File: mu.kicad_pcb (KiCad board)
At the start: 4 copper layers, 60 x 60 mm, 75 parts, among them J1 USB_C_Receptacle_USB2.0_16P, J2 Conn_02x03_Odd_Even, J4 2060-1452/998-404, J5 ESQ-110-X-X-D, U1 STM32F042F6P6, U10 TLV3603QDCKRQ1, U11 SN74LVC1G74DCUT, U12 LM4040AIM3-2.5/NOPB, U13 MCP4921-E/SN, U14 BMP390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

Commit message: routed fully, pending final checks
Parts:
- moved C21 0.50 mm to (146.5, 67.0), turned to 180 degrees
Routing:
- net SPI_CS_FLASH: track 10.7 -> 9.67 mm

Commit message: ready for review
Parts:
- added G***: LOGO, LOGO, F.Cu at (144.2, 79.0)
- added G***: LOGO, LOGO, F.Cu at (146.0, 80.0)
- added G***: LOGO, LOGO, B.Cu at (179.5, 89.5)
- added G***: LOGO, LOGO, B.Cu at (156.0, 79.0)
- added G***: LOGO, LOGO, B.Cu at (167.5, 72.5)
- added G***: LOGO, LOGO, B.Cu at (167.0, 101.0)
- added G***: LOGO, LOGO, B.Cu at (138.5, 75.0)
- added G***: LOGO, LOGO, B.Cu at (146.5, 79.0)
- added REF**: WEEE-Logo_5.6x8mm_SilkScreen, Symbol:WEEE-Logo_5.6x8mm_SilkScreen, B.Cu at (147.5, 55.5)
- added REF**: ESD-Logo_6.6x6mm_SilkScreen, Symbol:ESD-Logo_6.6x6mm_SilkScreen, B.Cu at (166.5, 55.5)

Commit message: programming stuff
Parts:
- added J3: Conn_02x03_Odd_Even, Connector_PinHeader_1.00mm:PinHeader_2x03_P1.00mm_Vertical, F.Cu at (154.4, 88.0)
- moved R10 0.88 mm to (152.0, 86.6)
- moved R12 0.88 mm to (154.5, 86.2)
- moved R13 0.88 mm to (155.5, 86.2)
- moved R6 0.33 mm to (156.1, 84.2)
- moved U1 0.33 mm to (160.0, 87.7)
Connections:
- net Net-(U1A-NRST) renamed NRST
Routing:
- net NRST: track 2.68 -> 8.94 mm, vias 0 -> 1
- net 3.3V_Dig: track 130.3 -> 136.2 mm
- net SWCLK: track 0.68 -> 4.65 mm
- net SWDIO: track 1.79 -> 4.56 mm
- net GND: track 49.6 -> 52.0 mm
- net VBUS_RAW: track 60.1 -> 60.9 mm

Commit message: indeed
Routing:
- net 3.3V_Dig: track 136.2 -> 130.9 mm, vias 10 -> 9
- net GND: vias 54 -> 63
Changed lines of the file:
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@@
+	)
+	(via
+		(at 145 96)
+		(size 0.6)
+		(drill 0.3)
+		(layers "F.Cu" "B.Cu")
+		(free yes)
+		(net 1)
 	)
 	(via
@@
 	)
 	(via
+		(at 154.5 93)
+		(size 0.6)
+		(drill 0.3)
+		(layers "F.Cu" "B.Cu")
+		(free yes)
+		(net 1)
+	)
+	(via
 		(at 150.5 60)
 		(size 0.6)
@@
 	)
 	(via
+		(at 141 82)
+		(size 0.6)
+		(drill 0.3)
+		(layers "F.Cu" "B.Cu")
+		(free yes)
+		(net 1)
+	)
+	(via
+		(at 170.5 67)
+		(size 0.6)
+		(drill 0.3)
+		(layers "F.Cu" "B.Cu")
+		(free yes)
+		(net 1)
+	)
+	(via
 		(at 155 72)
 		(size 0.6)
@@
 	)
 	(via
+		(at 159.5 63)
+		(size 0.6)
+		(drill 0.3)
+		(layers "F.Cu" "B.Cu")
+		(free yes)
+		(net 1)
+	)
+	(via
 		(at 146.575 59.356)
 		(size 0.6)
@@
 	)
 	(via
-		(at 163.545601 63.4861)
+		(at 152 83)
 		(size 0.6)
 		(drill 0.3)
@@
 	)
 	(via
+		(at 170.5 76.5)
+		(size 0.6)
+		(drill 0.3)
+		(layers "F.Cu" "B.Cu")
+		(free yes)
+		(net 1)
+	)
+	(via
 		(at 155.54 68.75)
 		(size 0.6)
@@
 	)
 	(via
+		(at 154.5 55.5)
+		(size 0.6)
+		(drill 0.3)
+		(layers "F.Cu" "B.Cu")
+		(free yes)
+		(net 1)
+	)
+	(via
 		(at 148.595 62.336)
 		(size 0.6)
@@
 	)
 	(via
+		(at 141 88.5)
+		(size 0.6)
+		(drill 0.3)
+		(layers "F.Cu" "B.Cu")
+		(free yes)
+		(net 1)
+	)
+	(via
 		(at 161 88.5)
 		(size 0.6)
@@
 		(layers "F.Cu" "B.Cu")
 		(free yes)
+		(net 1)
+	)
+	(via
+		(at 184 72.952)
+		(size 0.6)
+		(drill 0.3)
+		(layers "F.Cu" "B.Cu")
 		(net 1)
 	)
@@
 	)
 	(segment
+		(start 184 72.952)
+		(end 183.02 72.952)
+		(width 0.6)
+		(layer "B.Cu")
+		(net 1)
+	)
+	(segment
 		(start 159.711326 100.383399)
 		(end 159.711326 98.738399)
@@
 	(segment
 		(start 184.024 72.952)
-		(end 183.02 72.952)
+		(end 184 72.952)
 		(width 0.6)
 		(layer "B.Cu")
@@
 	)
 	(via
-		(at 148 74.5)
-		(size 0.6)
-		(drill 0.3)
-		(layers "F.Cu" "B.Cu")
-		(net 2)
-	)
-	(via
 		(at 159.474999 94.579)
 		(size 0.6)
@@
 	)
 	(segment
-		(start 148 74.5)
-		(end 147 75.5)
-		(width 0.25)
-		(layer "In1.Cu")
-		(net 2)
-	)
-	(segment
-		(start 157.5 73.5)
-		(end 157.5 71.75)
-		(width 0.25)
-		(layer "In1.Cu")
-		(net 2)
-	)
-	(segment
 		(start 166.293225 91.600756)
 		(end 164.915981 92.978)
@@
 	(segment
 		(start 157.5 71.75)
-		(end 156 70.25)
+		(end 157.5 75)
 		(width 0.25)
 		(layer "In1.Cu")
@@
 	)
 	(segment
+		(start 156 70.25)
+		(end 157.5 71.75)
+		(width 0.25)
+		(layer "In1.Cu")
+		(net 2)
+	)
+	(segment
 		(start 170 82.5)
 		(end 171 82.5)
@@
 	)
 	(segment
-		(start 157.101 73.899)
-		(end 152.101 73.899)
-		(width 0.25)
-		(layer "In1.Cu")
-		(net 2)
-	)
-	(segment
 		(start 166.293225 91.600756)
 		(end 166.5 91.393981)
@@
 	)
 	(segment
-		(start 152.101 73.899)
-		(end 151.5 74.5)
-		(width 0.25)
-		(layer "In1.Cu")
-		(net 2)
-	)
-	(segment
 		(start 159.299999 70.25)
 		(end 156 70.25)
@@
 	)
 	(segment
-		(start 157.5 73.5)
-		(end 157.101 73.899)
+		(start 157.5 75)
+		(end 147.5 85)
 		(width 0.25)
 		(layer "In1.Cu")
@@
 	)
 	(segment
+		(start 147.5 90.840598)
+		(end 147.365 90.975598)
+		(width 0.25)
+		(layer "In1.Cu")
+		(net 2)
+	)
+	(segment
 		(start 162 67.549999)
 		(end 159.299999 70.25)
@@
 	)
 	(segment
-		(start 147 75.5)
-		(end 147 90.610598)
-		(width 0.25)
-		(layer "In1.Cu")
-		(net 2)
-	)
-	(segment
 		(start 159.474999 94.579)
 		(end 160.075999 95.18)
@@
 	)
 	(segment
-		(start 151.5 74.5)
-		(end 148 74.5)
-		(width 0.25)
-		(layer "In1.Cu")
-		(net 2)
-	)
-	(segment
 		(start 163.05454 93.488)
 		(end 162.556654 93.488)
@@
 	)
 	(segment
+		(start 147.5 85)
+		(end 147.5 90.840598)
+		(width 0.25)
+		(layer "In1.Cu")
+		(net 2)
+	)
+	(segment
 		(start 162.556654 93.488)
 		(end 161.474999 94.569655)
 		(width 0.25)
 		(layer "In1.Cu")
-		(net 2)
-	)
-	(segment
-		(start 147 90.610598)
-		(end 147.365 90.975598)
-		(width 0.25)
-		(layer "In1.Cu")

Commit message: ready to send off to stephen
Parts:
- added G***: LOGO, LOGO, F.Cu at (146.5, 56.0)
- moved C3 8.27 mm to (154.1, 83.3), turned to 90 degrees
- moved C2 8.23 mm to (155.2, 83.3), turned to 90 degrees
- moved C1 5.41 mm to (156.2, 83.3), turned to 90 degrees
- moved R5 0.33 mm to (159.3, 82.7)
- moved C29 0.30 mm to (151.0, 60.7)
- moved C28 0.30 mm to (151.0, 61.7)
- moved C13 0.30 mm to (158.2, 82.7)
- moved FB1 0.27 mm to (160.4, 82.7)
- moved C9 0.26 mm to (162.4, 82.7)
- moved C8 0.25 mm to (161.4, 82.7)
- moved C19 0.25 mm to (150.3, 67.5)
- moved C22 0.23 mm to (149.3, 67.5)
- turned U3 to 180 degrees
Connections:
- J5 pad 13: unconnected-(J5-Pad13) -> GND
- U3 pad 1: Net-(U6-NONIINVERTINGINPUT) -> 2.5V_Ref
- U3 pad 2: unconnected-(U3-Pad2) -> Net-(U6-NONIINVERTINGINPUT)
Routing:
- net unconnected-(J5-Pad03): track 0.00 -> 10.2 mm
- net unconnected-(J5-Pad09): track 0.00 -> 10.2 mm
- net HV: track 23.5 -> 30.8 mm
- net 2.5V_Ref: track 8.52 -> 12.4 mm, vias 0 -> 1
- net SWDIO: track 4.56 -> 6.48 mm
- net Latch_Rst: track 26.0 -> 27.8 mm
- net 5V: track 90.0 -> 91.3 mm
- net NRST: track 8.94 -> 7.97 mm
- net SPI_MISO: track 21.1 -> 20.2 mm
- net Net-(U1B-VDDA): track 4.01 -> 4.84 mm
- net SPI_MOSI: track 43.5 -> 42.8 mm, vias 3 -> 2
- net PA+: track 12.1 -> 11.5 mm
- net Net-(J1-D--PadA7): track 5.43 -> 6.07 mm
- net PA-: track 11.7 -> 11.0 mm
- net GND: track 52.0 -> 52.5 mm

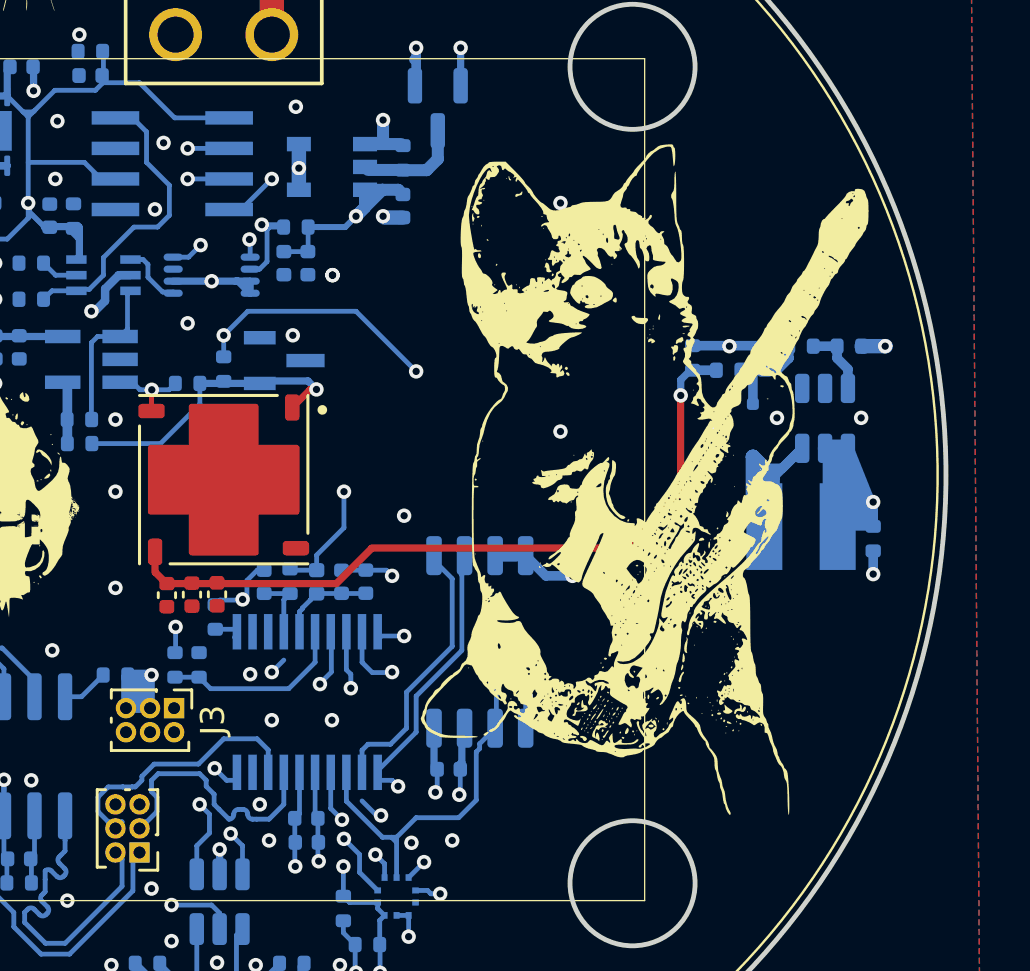
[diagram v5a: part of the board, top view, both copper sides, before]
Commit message: higher voltage diode
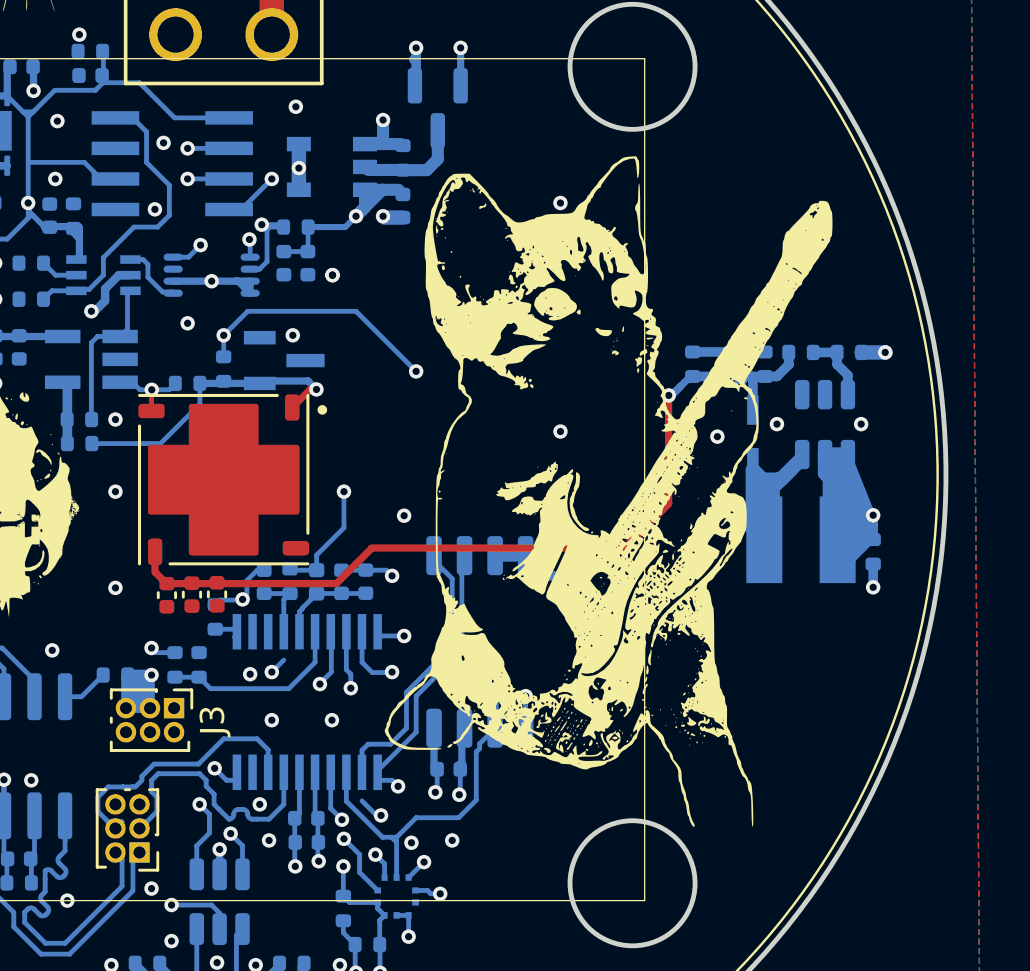
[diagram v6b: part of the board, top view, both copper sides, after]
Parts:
- removed D1: BAT54J, Diode_SMD:D_SOD-323F
- added CR1: BAT46JFILM, footprints:SOD-323_STM, B.Cu at (178.5, 76.7)
- moved G*** 1.58 mm to (171.8, 78.5)
- moved C7 0.55 mm to (183.5, 81.5)
- moved L1 0.55 mm to (180.5, 81.0)
- moved C10 0.26 mm to (176.0, 73.7)
- moved C4 0.26 mm to (179.0, 73.7)
- moved R1 0.26 mm to (180.5, 73.2)
- moved R2 0.26 mm to (182.5, 73.2)
- moved R4 0.26 mm to (177.5, 74.2)
- moved U2 0.26 mm to (181.5, 76.2)
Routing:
- net 5V: track 91.3 -> 93.6 mm
- net Net-(U2-LX): track 14.5 -> 16.5 mm
- net VBUS_RAW: track 60.9 -> 62.0 mm
